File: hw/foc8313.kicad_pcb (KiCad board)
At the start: 4 copper layers, 35 x 35 mm, 85 parts, among them J1 Tag Connect, J2 CAN, J3 CAN, J4 Aux, P1 USB_C_Plug, SW1 SW_SPST, U1 DRV8313PWP, U10 XC6206P332MR, U11 TJA1051TK/3,118, U12 ADUM1201ARZ-RL7, U13 XC6206P332MR, U2 STM32F103CBTx, U3 AS5047D, U4 INA240A2D, U5 INA240A2D, U6 AT24C256C-SSHL-T, U7 LMR36015SFBRNXR, U8 INA240A2D, X1 X322516MLB4SI

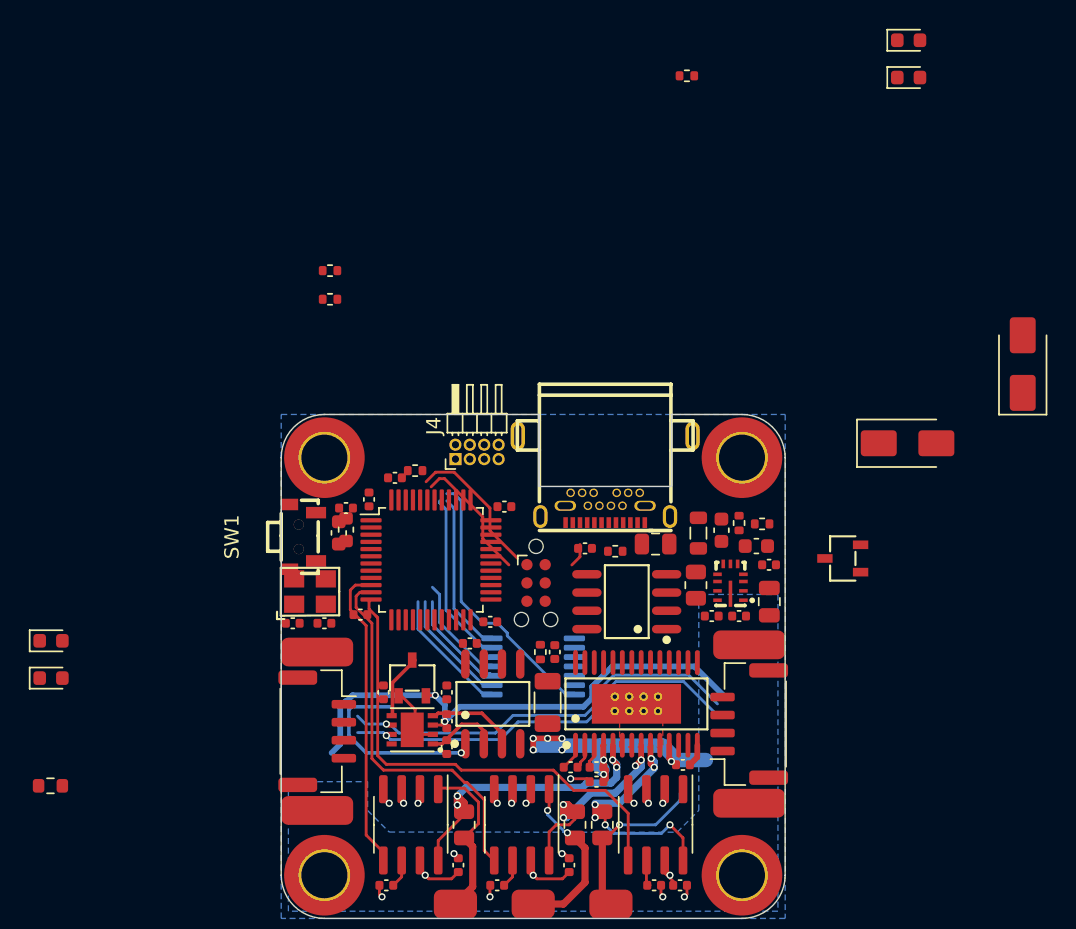
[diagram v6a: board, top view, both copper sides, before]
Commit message: [Hw] Tiny eeprom, all components fit on board!
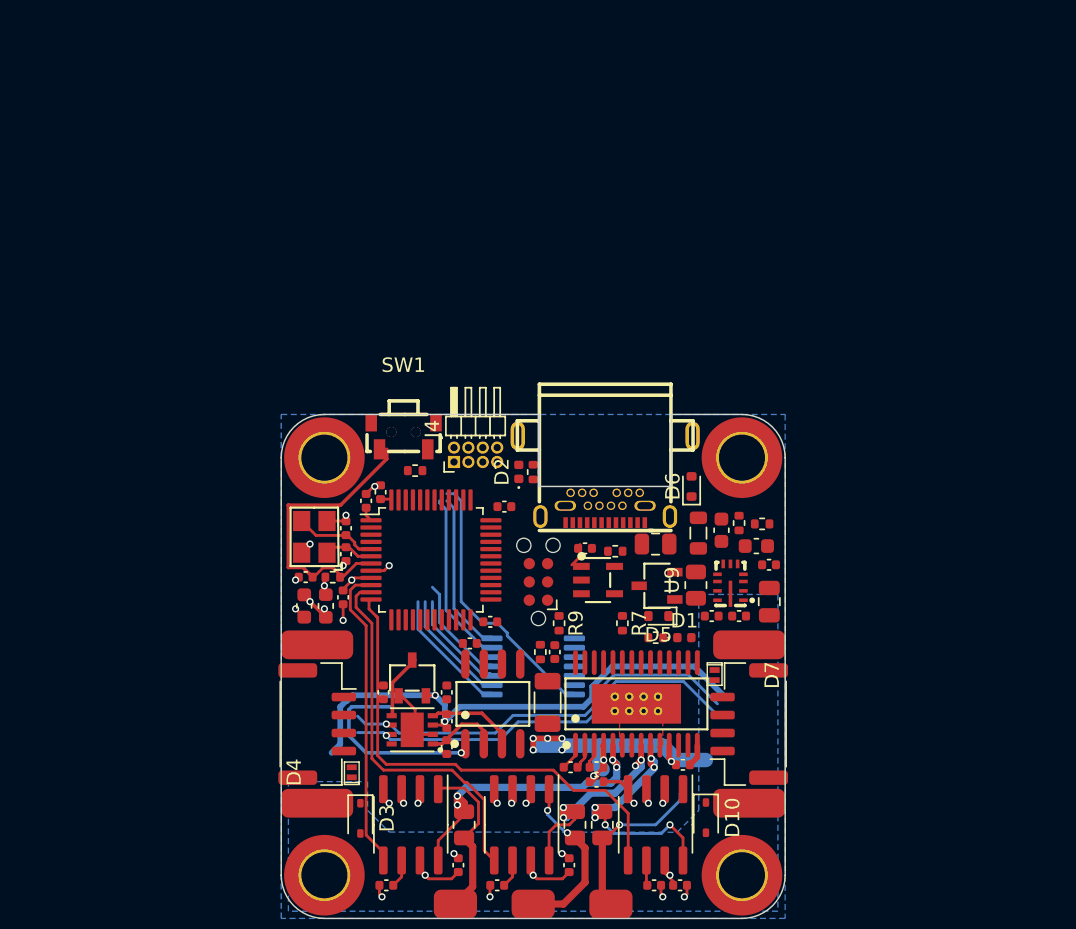
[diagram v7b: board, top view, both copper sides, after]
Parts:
- removed D8: BLUE, LED_SMD:LED_0603_1608Metric
- removed U6: AT24C256C-SSHL-T, easyeda:SOIC-8_L4.9-W3.9-P1.27-LS6.0-BL
- added D10: 36V, Diode_SMD:D_SOD-323, F.Cu at (152.0, 110.5)
- added D3: 36V, Diode_SMD:D_SOD-323, F.Cu at (128.0, 110.5)
- added D7: 5V, easyeda:X1-DFN1006-2_L1.0-W0.6-RD, F.Cu at (152.6, 100.6)
- added R7: 10k, Resistor_SMD:R_0402_1005Metric, F.Cu at (146.2, 97.0)
- added U9: ZD24C08AE1-STGMT, easyeda:SOT-23-5_L3.0-W1.7-P0.95-LS2.8-BL, F.Cu at (144.5, 94.0)
- D1: footprint Diode_SMD:D_0603_1608Metric -> Diode_SMD:D_0402_1005Metric
- D2: footprint LED_SMD:LED_0603_1608Metric -> LED_SMD:LED_0402_1005Metric
- D4: footprint Diode_SMD:D_0603_1608Metric -> easyeda:X1-DFN1006-2_L1.0-W0.6-RD
- D5, D6: value SS210 -> RB521S30T1G; footprint Diode_SMD:D_SMA -> Diode_SMD:D_SOD-523
- R9: value 1k5 -> 10k; footprint Resistor_SMD:R_0603_1608Metric -> Resistor_SMD:R_0402_1005Metric
- moved D1 44.3 mm to (150.5, 98.0)
- moved R2 39.1 mm to (148.5, 98.0)
- moved D2 38.5 mm to (139.0, 86.5), turned to 90 degrees
- moved R9 37.1 mm to (141.8, 97.0), turned to -90 degrees
- moved D5 30.8 mm to (148.7, 96.5), turned to 180 degrees
- moved D4 22.8 mm to (127.4, 107.3), turned to 90 degrees
- moved R1 21.3 mm to (126.1, 93.8)
- moved R5 18.5 mm to (140.0, 86.5), turned to -90 degrees
- moved D6 15.3 mm to (151.0, 87.5), turned to 90 degrees
- moved U10 13.0 mm to (148.6, 94.4)
- moved SW1 9.90 mm to (131.0, 84.0), turned to 0 degrees
- moved C14 7.57 mm to (127.0, 90.4), turned to 90 degrees
- moved C5 5.61 mm to (124.1, 95.8), turned to -90 degrees
- moved C9 5.56 mm to (124.2, 93.8), turned to 180 degrees
- moved L2 5.48 mm to (125.6, 95.8), turned to 90 degrees
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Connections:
- C1 pad 2: +3V3 -> GND
- C10 pad 2: +3V3 -> GND
- C11 pad 2: +3V3 -> GND
- C12 pad 2: +3V3 -> GND
- C13 pad 2: +3V3 -> GND
- C14 pad 2: +3V3 -> GND
- C15 pad 1: +3V3 -> GND
- C16 pad 2: +3V3 -> GND
- C17 pad 2: +3V3 -> GND
- C19 pad 2: +3V3 -> GND
- C2 pad 2: +3V3 -> GND
- C20 pad 2: +3V3 -> GND
- C22 pad 2: +3V3 -> GND
- C23 pad 2: +3V3 -> GND
- C24 pad 2: +3V3 -> GND
- C25 pad 1: +3V3 -> +3.3V
- C25 pad 2: Net-(U6-VCC) -> GND
- C26 pad 2: +3V3 -> GND
- C27 pad 2: +3V3 -> GND
- C29 pad 2: +3V3 -> GND
- C30 pad 2: +3V3 -> GND
- C31 pad 2: +3V3 -> GND
- C33 pad 2: +3V3 -> GND
- C4 pad 2: +3V3 -> GND
- C5 pad 2: +3V3 -> GND
- C6 pad 2: +3V3 -> GND
- C7 pad 2: +3V3 -> GND
- C9 pad 2: +3V3 -> GND
- H5 pad 1: +3V3 -> GND
- H7 pad 1: +3V3 -> GND
- J1 pad 5: +3V3 -> GND
- L2 pad 2: +3V3 -> +3.3V
- P1 pad A1: +3V3 -> GND
- P1 pad A12: +3V3 -> GND
- P1 pad B1: +3V3 -> GND
- P1 pad B12: +3V3 -> GND
- R11 pad 2: +3V3 -> GND
- R13 pad 2: +3V3 -> GND
- R3 pad 1: +3V3 -> GND
- R5 pad 2: +3V3 -> GND
- R9 pad 1: Net-(D8-K) -> +3.3V
- R9 pad 2: +3V3 -> /I2C.SCL
- SW1 pad 1: +3V3 -> /~{NRST}
- SW1 pad 2: /~{NRST} -> GND
- U1 pad 10: +3V3 -> GND
- U1 pad 14: +3V3 -> GND
- U1 pad 20: +3V3 -> GND
- U1 pad 28: +3V3 -> GND
- U1 pad 29: +3V3 -> GND
- U1 pad 6: +3V3 -> GND
- U1 pad 7: +3V3 -> GND
- U10 pad 1: +3V3 -> GND
- U12 pad 5: +3V3 -> GND
- U2 pad 23: +3V3 -> GND
- U2 pad 35: +3V3 -> GND
- U2 pad 47: +3V3 -> GND
- U2 pad 8: GNDA -> GND
- U3 pad 13: +3V3 -> GND
- U3 pad 5: +3V3 -> GND
- U4 pad 2: +3V3 -> GND
- U4 pad 3: +3V3 -> GND
- U4 pad 4: +3V3 -> GND
- U5 pad 2: +3V3 -> GND
- U5 pad 3: +3V3 -> GND
- U5 pad 4: +3V3 -> GND
- U7 pad 1: +3V3 -> GND
- U7 pad 11: +3V3 -> GND
- U7 pad 6: +3V3 -> GND
- U8 pad 2: +3V3 -> GND
- U8 pad 3: +3V3 -> GND
- U8 pad 4: +3V3 -> GND
- X1 pad 2: +3V3 -> GND
- X1 pad 4: +3V3 -> GND
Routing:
- net GND: track 0.00 -> 25.1 mm, vias 0 -> 23
- net /~{NRST}: track 0.00 -> 19.9 mm
- net +3V3: track 18.7 -> 0.00 mm, vias 16 -> 0
- net /USB_DP: track 10.0 -> 0.00 mm
- net /USB_DM: track 9.01 -> 0.00 mm
- net /HSE_IN: track 0.00 -> 5.72 mm
- net +3.3VA: track 9.75 -> 14.9 mm, vias 3 -> 6
- net +3.3V: track 5.77 -> 10.5 mm, vias 0 -> 1
- net /HSE_OUT: track 0.00 -> 3.48 mm
- net /PHC: track 16.8 -> 18.6 mm
- net /PHB: track 15.5 -> 16.8 mm
- net VCC: track 22.9 -> 23.7 mm
- added copper zone on B.Cu, net GND
- added copper zone on In1.Cu, net GND
- added copper zone on In2.Cu, net GND
- removed copper zone on B.Cu, net +3V3
- removed copper zone on In1.Cu, net +3V3
- removed copper zone on In2.Cu, net +3V3

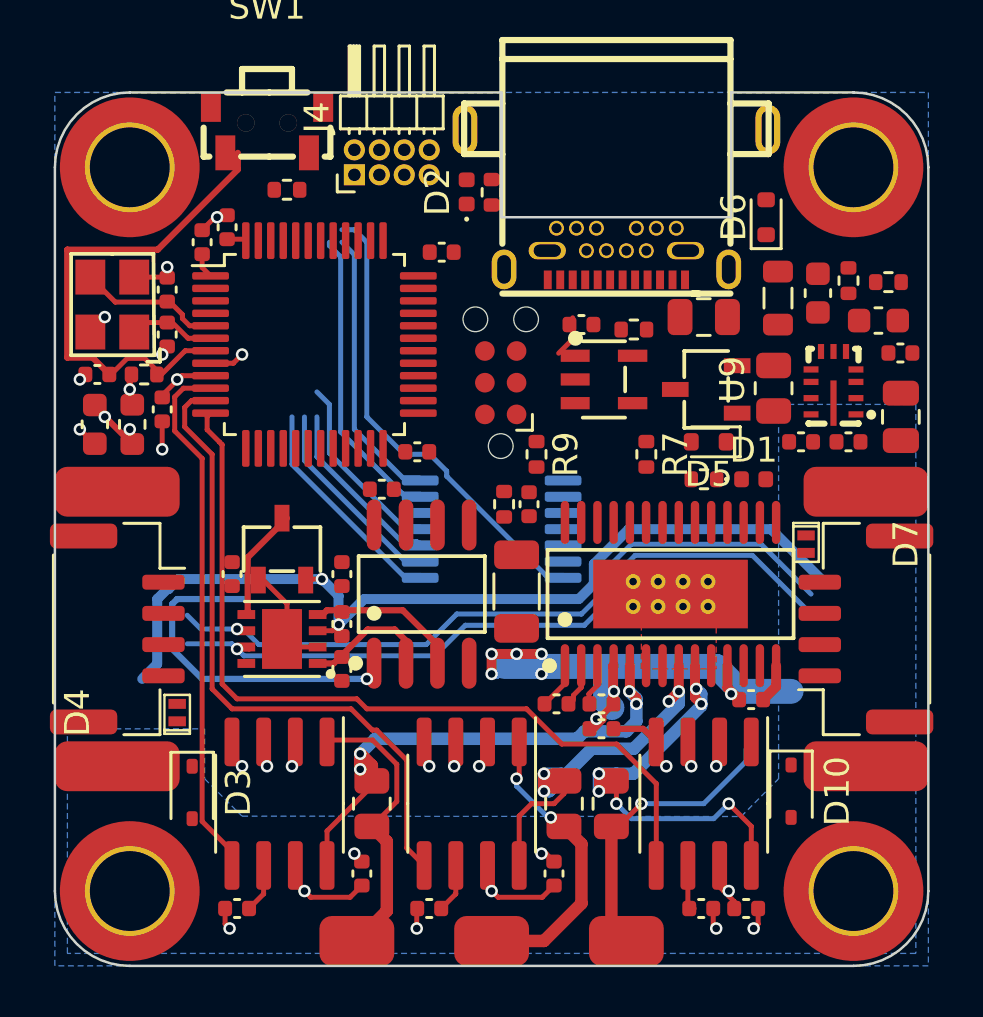
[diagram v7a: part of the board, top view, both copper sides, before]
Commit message: [Hw] Simplifying CAN
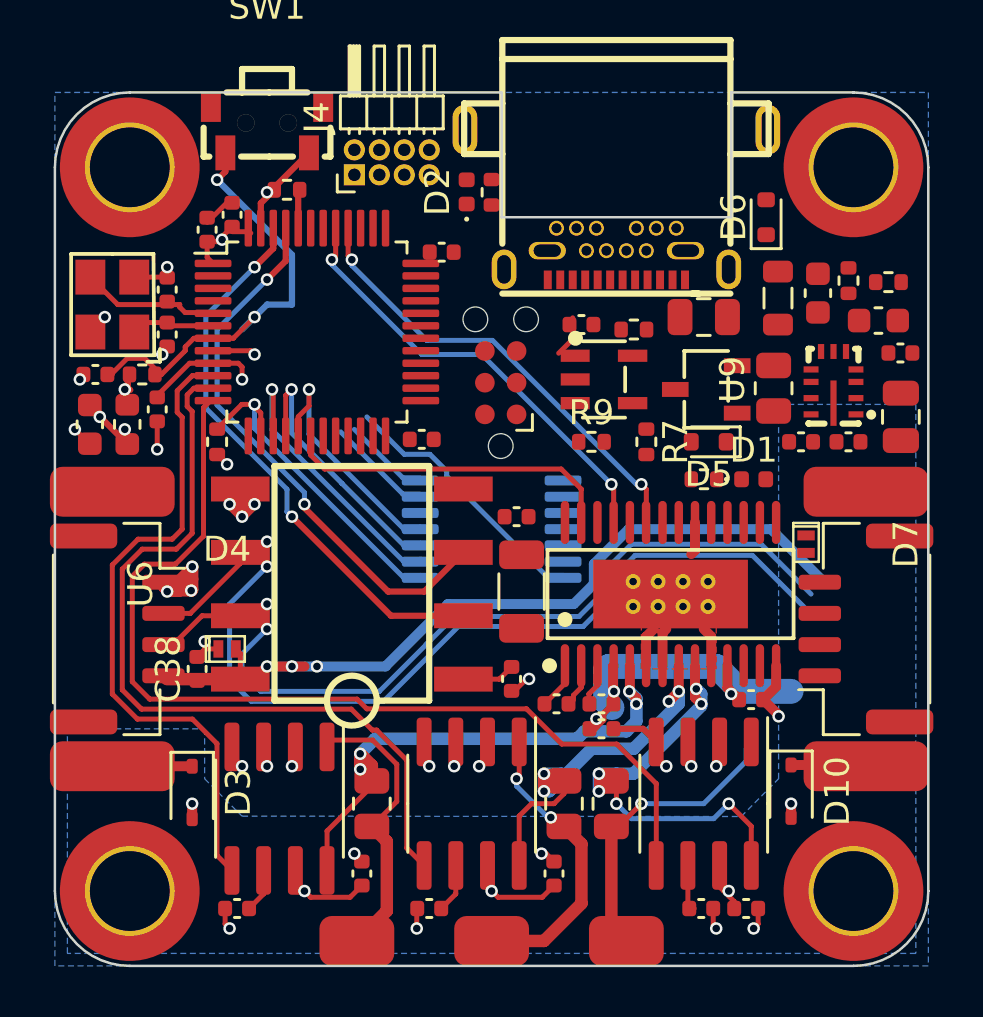
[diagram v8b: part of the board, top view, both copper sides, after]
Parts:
- removed C32, C34, C35: 100n, Capacitor_SMD:C_0402_1005Metric
- removed U11: TJA1051TK/3,118, easyeda:HVSON-8_L3.0-W3.0-P0.65-BL-EP
- removed U12: ADUM1201ARZ-RL7, easyeda:SOIC-8_L4.9-W3.9-P1.27-LS6.0-BL
- removed U13: XC6206P332MR, easyeda:SOT-23-3_L2.9-W1.6-P1.90-LS2.8-BR
- added U6: ISO1050DUBR, easyeda:SOIC-8_L9.3-W6.6-P2.54-LS10.4-BL, F.Cu at (134.4, 102.2)
- moved R6 11.8 mm to (129.0, 96.5)
- moved C33 9.21 mm to (140.8, 106.0), turned to -90 degrees
- moved C38 6.93 mm to (128.2, 105.6), turned to 90 degrees
- moved D4 3.24 mm to (129.4, 104.8), turned to 0 degrees
- moved R9 2.26 mm to (144.0, 96.5), turned to 0 degrees
- moved C7 0.71 mm to (141.0, 99.5), turned to 180 degrees
- moved C12 0.54 mm to (128.6, 88.0)
- moved C13 0.54 mm to (129.6, 87.4)
- moved C10 0.53 mm to (137.2, 96.4)
- moved U2 0.51 mm to (133.0, 92.1)
- moved R7 0.50 mm to (146.2, 96.5)
- moved C6 0.20 mm to (126.6, 95.2)
- moved H4 0.20 mm to (124.8, 109.5)
- moved H7 0.20 mm to (124.8, 98.5)
- moved U4 0.20 mm to (131.5, 111.2)
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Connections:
- U1 pad 23: /DRV_INC -> /DRV_INA
- U1 pad 27: /DRV_INA -> /DRV_INC
- U1 pad 5: /PHA -> /PHC
- U1 pad 9: /PHC -> /PHA
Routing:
- net /CAN.TX: track 0.00 -> 22.7 mm, vias 0 -> 2
- net /CAN.RX: track 0.00 -> 22.2 mm, vias 0 -> 2
- net /DRV_INA: track 0.00 -> 18.4 mm, vias 0 -> 2
- net /DRV_INB: track 0.00 -> 18.0 mm, vias 0 -> 2
- net Net-(U11-VIO): track 17.8 -> 0.00 mm, vias 1 -> 0
- net GND: track 25.1 -> 38.7 mm, vias 23 -> 27
- net /DRV_INC: track 0.00 -> 13.5 mm
- net /CAN.L: track 29.0 -> 38.0 mm, vias 1 -> 2
- net /ENC_Z: track 18.8 -> 10.6 mm
- net /CAN.V-: track 4.32 -> 12.3 mm, vias 0 -> 7
- net /ENC_B: track 12.0 -> 4.22 mm
- net /ENC_A: track 11.2 -> 3.45 mm
- net Net-(U11-RXD): track 5.98 -> 0.00 mm
- net /ISENSE_C: track 33.5 -> 39.3 mm
- net /ISENSE_B: track 26.4 -> 32.1 mm
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- added copper zone on In1.Cu, net /CAN.V-
